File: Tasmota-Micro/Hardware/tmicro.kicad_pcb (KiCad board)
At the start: 2 copper layers, 33.5 x 13 mm, 16 parts, among them P2 CONN_01X02, P3 CONN_01X02, P4 CONN_01X04, P5 CONN_01X02, P6 CONN_01X02, P7 USB_A, Q1 IRLML6244, Q2 IRLML6244, U1 MCP1703, U2 ESP-01v090

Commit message: removed the confusing cache form the name
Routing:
- net Net-(R3-Pad1): track 11.1 -> 7.77 mm
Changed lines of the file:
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@@
 (kicad_pcb (version 4) (host pcbnew 4.0.2+dfsg1-stable)
   (general
-    (links 31)
-    (no_connects 1)
+    (links 0)
+    (no_connects 0)
     (area 144.407 102.575 201.425001 126.875)
     (thickness 1.6)
     (drawings 14)
-    (tracks 99)
+    (tracks 97)
     (zones 0)
     (modules 16)
@@
   (segment (start 169.95 115.201) (end 169.95 115.2008) (width 0.25) (layer F.Cu) (net 2) (status 30))
   (segment (start 158.22502 115.12502) (end 158.22502 115.010088) (width 0.4) (layer B.Cu) (net 3))
-  (segment (start 159.4 115.25) (end 158.35 115.25) (width 0.4) (layer B.Cu) (net 3))
+  (segment (start 159.4 115.25) (end 158.35 115.25) (width 0.4) (layer B.Cu) (net 3) (status 10))
   (via (at 158.22502 115.010088) (size 0.6) (drill 0.4) (layers F.Cu B.Cu) (net 3))
   (segment (start 158.35 115.25) (end 158.22502 115.12502) (width 0.4) (layer B.Cu) (net 3))
@@
   (segment (start 152.1 111.1664) (end 152.5464 110.72) (width 0.25) (layer F.Cu) (net 7))
   (segment (start 152.5464 110.72) (end 153.66 110.72) (width 0.25) (layer F.Cu) (net 7) (status 20))
-  (segment (start 165.58 118.8) (end 165.58 117.534) (width 0.25) (layer B.Cu) (net 8))
+  (segment (start 165.58 118.8) (end 165.58 117.534) (width 0.25) (layer B.Cu) (net 8) (status 10))
   (segment (start 165.58 117.534) (end 165.246 117.2) (width 0.25) (layer B.Cu) (net 8))
   (segment (start 165.246 117.2) (end 159 117.2) (width 0.25) (layer B.Cu) (net 8))
-  (segment (start 157.6 114.66) (end 156.2 113.26) (width 0.25) (layer B.Cu) (net 8))
+  (segment (start 157.6 114.66) (end 156.2 113.26) (width 0.25) (layer B.Cu) (net 8) (status 20))
   (segment (start 159 117.2) (end 157.6 115.8) (width 0.25) (layer B.Cu) (net 8))
   (segment (start 157.6 115.8) (end 157.6 114.66) (width 0.25) (layer B.Cu) (net 8))
@@
   (segment (start 177.8998 113.202) (end 174.848 113.202) (width 0.8) (layer F.Cu) (net 11) (status 30))
   (segment (start 177.8998 113.202) (end 177.9 113.2018) (width 0.25) (layer F.Cu) (net 11) (status 30))
-  (segment (start 154.5517 112.0711) (end 153.66 112.0711) (width 0.25) (layer B.Cu) (net 12))
-  (segment (start 154.8489 111.7739) (end 154.5517 112.0711) (width 0.25) (layer B.Cu) (net 12))
-  (segment (start 154.8489 110.3662) (end 154.8489 111.7739) (width 0.25) (layer B.Cu) (net 12))
-  (segment (start 155.6966 109.5185) (end 154.8489 110.3662) (width 0.25) (layer B.Cu) (net 12))
-  (segment (start 156.7485 109.5185) (end 155.6966 109.5185) (width 0.25) (layer B.Cu) (net 12))
-  (segment (start 159.4 112.17) (end 156.7485 109.5185) (width 0.25) (layer B.Cu) (net 12))
-  (segment (start 159.4 113.35) (end 159.4 112.17) (width 0.25) (layer B.Cu) (net 12) (status 10))
-  (segment (start 153.66 113.26) (end 153.66 112.0711) (width 0.25) (layer B.Cu) (net 12) (status 10))
+  (segment (start 158.7 111.6) (end 159.4 112.3) (width 0.25) (layer B.Cu) (net 12))
+  (segment (start 159.4 112.3) (end 159.4 113.35) (width 0.25) (layer B.Cu) (net 12))
+  (segment (start 157.8 111.6) (end 158.7 111.6) (width 0.25) (layer B.Cu) (net 12))
+  (segment (start 157.4 112) (end 157.8 111.6) (width 0.25) (layer B.Cu) (net 12))
+  (segment (start 154.92 112) (end 157.4 112) (width 0.25) (layer B.Cu) (net 12))
+  (segment (start 153.66 113.26) (end 154.92 112) (width 0.25) (layer B.Cu) (net 12))
   (segment (start 180.2 111.6) (end 180.8 111) (width 1.2) (layer B.Cu) (net 13) (status 20))
   (segment (start 178.099 111.6) (end 180.2 111.6) (width 1.2) (layer B.Cu) (net 13))

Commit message: updated with better zone fills
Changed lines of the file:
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@@
 (kicad_pcb (version 4) (host pcbnew 4.0.2+dfsg1-stable)
   (general
-    (links 0)
+    (links 31)
     (no_connects 0)
     (area 144.407 102.575 201.425001 126.875)
@@
     (user_trace_width 1.2)
     (trace_clearance 0.2)
-    (zone_clearance 0.2)
+    (zone_clearance 0.25)
     (zone_45_only no)
     (trace_min 0.2)
@@
   (gr_line (start 184.9 121) (end 184.9 108) (layer Edge.Cuts) (width 0.15))
   (segment (start 167.26 110.2) (end 169.8 110.2) (width 1.2) (layer B.Cu) (net 1) (status 30))
-  (segment (start 173.601 114.001) (end 169.8 110.2) (width 1.2) (layer B.Cu) (net 1) (status 30))
+  (segment (start 173.601 114.001) (end 169.8 110.2) (width 1.6) (layer B.Cu) (net 1) (status 30))
   (segment (start 173.601 114.2) (end 173.601 114.001) (width 1.2) (layer B.Cu) (net 1) (status 30))
   (segment (start 167.26 112.016) (end 167.26 110.2) (width 0.8) (layer F.Cu) (net 1) (status 20))
@@
   (segment (start 177.599 114.2) (end 177.599 112.1) (width 1.2) (layer B.Cu) (net 13) (status 10))
   (zone (net 2) (net_name GND) (layer B.Cu) (hatch edge 0.508)
-    (connect_pads yes (clearance 0.2))
+    (connect_pads yes (clearance 0.25))
     (min_thickness 0.2)
-    (fill yes (arc_segments 16) (thermal_gap 0.508) (thermal_bridge_width 0.508))
+    (fill yes (arc_segments 32) (thermal_gap 0.508) (thermal_bridge_width 0.508))
     (polygon
       (pts
@@
   )
   (zone (net 1) (net_name VPP) (layer F.Cu) (hatch edge 0.508)
-    (connect_pads yes (clearance 0.2))
+    (connect_pads yes (clearance 0.25))
     (min_thickness 0.2)
-    (fill yes (arc_segments 16) (thermal_gap 0.508) (thermal_bridge_width 0.508))
+    (fill yes (arc_segments 32) (thermal_gap 0.508) (thermal_bridge_width 0.508))
     (polygon
       (pts
@@
   )
   (zone (net 3) (net_name +3V3) (layer F.Cu) (hatch edge 0.508)
-    (connect_pads yes (clearance 0.2))
+    (connect_pads yes (clearance 0.25))
     (min_thickness 0.2)
-    (fill yes (arc_segments 16) (thermal_gap 0.508) (thermal_bridge_width 0.508))
+    (fill yes (arc_segments 32) (thermal_gap 0.508) (thermal_bridge_width 0.508))
     (polygon
       (pts

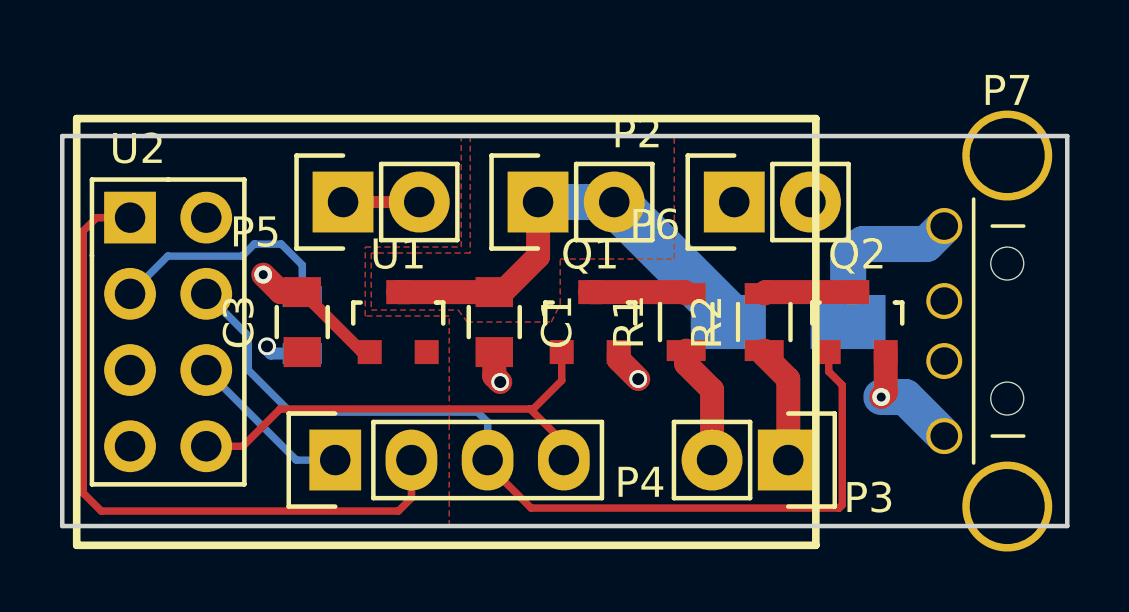
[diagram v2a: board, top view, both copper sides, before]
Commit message: 4 layers
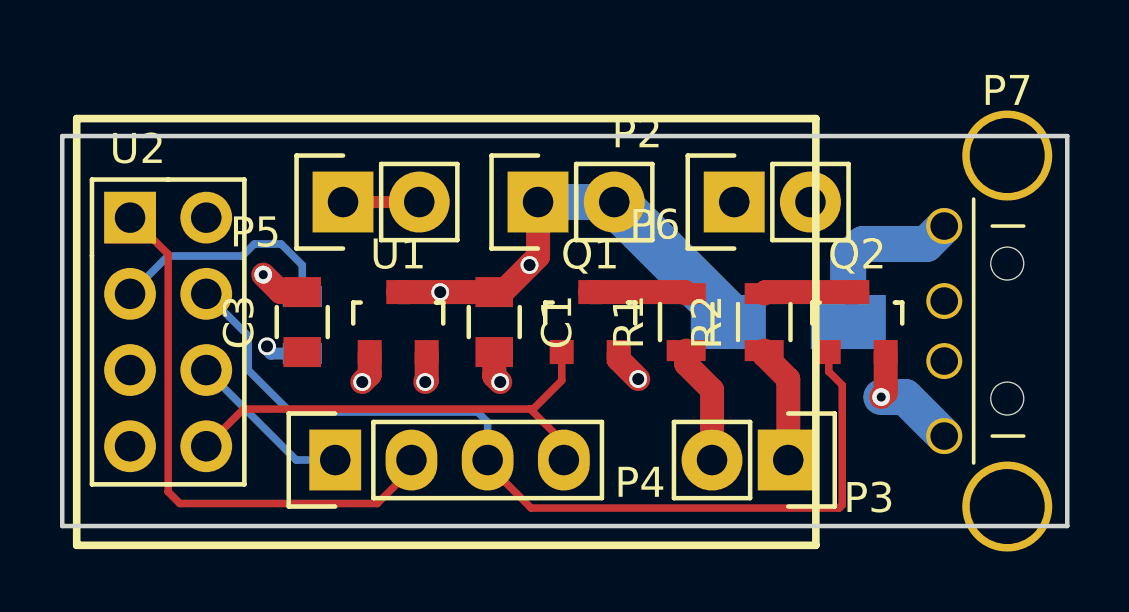
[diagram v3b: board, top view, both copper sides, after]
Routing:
- net TX: track 23.1 -> 19.8 mm
- net GND: track 11.4 -> 9.39 mm, vias 4 -> 5
- net +3V3: track 4.73 -> 5.75 mm, vias 1 -> 2
- net VPP: vias 0 -> 2
- added copper zone on In1.Cu, net +3V3
- added copper zone on In2.Cu, net GND
- added copper zone on In1.Cu, net VPP
- removed copper zone on F.Cu, net +3V3
- removed copper zone on B.Cu, net GND
- removed copper zone on F.Cu, net VPP
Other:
- copper layers 2 -> 4
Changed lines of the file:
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@@
   (general
     (links 31)
-    (no_connects 0)
+    (no_connects 1)
     (area 144.407 102.575 201.425001 126.875)
     (thickness 1.6)
     (drawings 14)
-    (tracks 97)
+    (tracks 107)
     (zones 0)
     (modules 16)
@@
   (layers
     (0 F.Cu signal)
+    (1 In1.Cu signal)
+    (2 In2.Cu signal)
     (31 B.Cu signal)
     (32 B.Adhes user)
@@
     (34 B.Paste user)
     (35 F.Paste user)
-    (36 B.SilkS user hide)
-    (37 F.SilkS user hide)
+    (36 B.SilkS user)
+    (37 F.SilkS user)
     (38 B.Mask user)
     (39 F.Mask user)
@@
   (gr_line (start 184.9 108) (end 151.4 108) (layer Edge.Cuts) (width 0.15))
   (gr_line (start 184.9 121) (end 184.9 108) (layer Edge.Cuts) (width 0.15))
+  (via (at 166.976 112.3) (size 0.6) (drill 0.4) (layers F.Cu B.Cu) (net 1))
+  (via (at 164 113.202) (size 0.6) (drill 0.4) (layers F.Cu B.Cu) (net 1))
+  (segment (start 166.976 112.3) (end 167.26 112.016) (width 0.8) (layer F.Cu) (net 1))
+  (segment (start 166.076 113.2) (end 166.976 112.3) (width 0.8) (layer F.Cu) (net 1) (status 10))
+  (segment (start 164 113.202) (end 165.798 113.202) (width 0.8) (layer F.Cu) (net 1) (status 20))
+  (segment (start 162.6002 113.202) (end 164 113.202) (width 0.8) (layer F.Cu) (net 1) (status 10))
   (segment (start 167.26 110.2) (end 169.8 110.2) (width 1.2) (layer B.Cu) (net 1) (status 30))
   (segment (start 173.601 114.001) (end 169.8 110.2) (width 1.6) (layer B.Cu) (net 1) (status 30))
   (segment (start 173.601 114.2) (end 173.601 114.001) (width 1.2) (layer B.Cu) (net 1) (status 30))
   (segment (start 167.26 112.016) (end 167.26 110.2) (width 0.8) (layer F.Cu) (net 1) (status 20))
-  (segment (start 166.076 113.2) (end 167.26 112.016) (width 0.8) (layer F.Cu) (net 1) (status 10))
   (segment (start 165.8 113.2) (end 166.076 113.2) (width 0.8) (layer F.Cu) (net 1) (status 30))
   (segment (start 162.6 113.202) (end 162.6002 113.202) (width 0.8) (layer F.Cu) (net 1) (status 30))
   (segment (start 165.798 113.202) (end 165.8 113.2) (width 0.8) (layer F.Cu) (net 1) (status 30))
-  (segment (start 162.6002 113.202) (end 165.798 113.202) (width 0.8) (layer F.Cu) (net 1) (status 30))
   (segment (start 162.6002 113.202) (end 162.6 113.2018) (width 0.25) (layer F.Cu) (net 1) (status 30))
-  (segment (start 161.65 115.20076) (end 161.40076 115.20076) (width 0.4) (layer F.Cu) (net 2) (status 30))
-  (segment (start 161.40076 115.20076) (end 159.4 113.2) (width 0.4) (layer F.Cu) (net 2) (status 30))
+  (segment (start 161.65 115.20076) (end 161.65 115.95) (width 0.8) (layer F.Cu) (net 2) (status 10))
+  (segment (start 161.65 115.95) (end 161.4 116.2) (width 0.8) (layer F.Cu) (net 2))
+  (via (at 161.4 116.2) (size 0.6) (drill 0.4) (layers F.Cu B.Cu) (net 2))
   (segment (start 161.65 115.20076) (end 161.60076 115.20076) (width 0.4) (layer F.Cu) (net 2) (status 30))
   (segment (start 169.95 115.20076) (end 169.95 115.45) (width 0.8) (layer F.Cu) (net 2) (status 30))
@@
   (segment (start 178.85 115.201) (end 178.85 115.2008) (width 0.25) (layer F.Cu) (net 2) (status 30))
   (segment (start 169.95 115.201) (end 169.95 115.2008) (width 0.25) (layer F.Cu) (net 2) (status 30))
+  (segment (start 163.55 115.20076) (end 163.55 116.15) (width 0.8) (layer F.Cu) (net 3) (status 10))
+  (segment (start 163.55 116.15) (end 163.5 116.2) (width 0.8) (layer F.Cu) (net 3))
+  (via (at 163.5 116.2) (size 0.6) (drill 0.4) (layers F.Cu B.Cu) (net 3))
   (segment (start 158.22502 115.12502) (end 158.22502 115.010088) (width 0.4) (layer B.Cu) (net 3))
   (segment (start 159.4 115.25) (end 158.35 115.25) (width 0.4) (layer B.Cu) (net 3) (status 10))
@@
   (segment (start 159.2 118.8) (end 156.2 115.8) (width 0.25) (layer B.Cu) (net 6) (status 20))
   (segment (start 160.5 118.8) (end 159.2 118.8) (width 0.25) (layer B.Cu) (net 6) (status 10))
-  (segment (start 163.04 120.066) (end 162.606 120.5) (width 0.25) (layer F.Cu) (net 7))
-  (segment (start 163.04 118.8) (end 163.04 120.066) (width 0.25) (layer F.Cu) (net 7) (status 10))
-  (segment (start 162.606 120.5) (end 152.7 120.5) (width 0.25) (layer F.Cu) (net 7))
-  (segment (start 152.7 120.5) (end 152.1 119.9) (width 0.25) (layer F.Cu) (net 7))
-  (segment (start 152.1 119.9) (end 152.1 111.1664) (width 0.25) (layer F.Cu) (net 7))
-  (segment (start 152.1 111.1664) (end 152.5464 110.72) (width 0.25) (layer F.Cu) (net 7))
-  (segment (start 152.5464 110.72) (end 153.66 110.72) (width 0.25) (layer F.Cu) (net 7) (status 20))
+  (segment (start 153.66 110.72) (end 153.71 110.72) (width 0.25) (layer F.Cu) (net 7))
+  (segment (start 155.32 120.25) (end 161.9 120.25) (width 0.25) (layer F.Cu) (net 7))
+  (segment (start 153.71 110.72) (end 154.93 111.94) (width 0.25) (layer F.Cu) (net 7))
+  (segment (start 154.93 111.94) (end 154.93 119.86) (width 0.25) (layer F.Cu) (net 7))
+  (segment (start 154.93 119.86) (end 155.32 120.25) (width 0.25) (layer F.Cu) (net 7))
+  (segment (start 163.04 119.11) (end 163.04 118.8) (width 0.25) (layer F.Cu) (net 7))
+  (segment (start 161.9 120.25) (end 163.04 119.11) (width 0.25) (layer F.Cu) (net 7))
+  (segment (start 153.66 110.72) (end 153.66 110.86) (width 0.25) (layer F.Cu) (net 7) (status 30))
+  (segment (start 163.04 117.94) (end 163.04 118.8) (width 0.25) (layer F.Cu) (net 7) (status 30))
+  (segment (start 163.04 118.8) (end 162.964602 118.8) (width 0.25) (layer F.Cu) (net 7) (status 30))
   (segment (start 165.58 118.8) (end 165.58 117.534) (width 0.25) (layer B.Cu) (net 8) (status 10))
   (segment (start 165.58 117.534) (end 165.246 117.2) (width 0.25) (layer B.Cu) (net 8))
@@
   (segment (start 177.3 120.4) (end 167.0276 120.4) (width 0.25) (layer F.Cu) (net 8))
   (segment (start 167.0276 120.4) (end 165.58 118.9524) (width 0.25) (layer F.Cu) (net 8) (status 20))
+  (segment (start 167 117.1) (end 157.44 117.1) (width 0.25) (layer F.Cu) (net 9))
+  (segment (start 157.44 117.1) (end 156.2 118.34) (width 0.25) (layer F.Cu) (net 9))
   (segment (start 167 117.1) (end 167.1 117.1) (width 0.25) (layer F.Cu) (net 9))
   (segment (start 167.1 117.1) (end 168.05 116.15) (width 0.25) (layer F.Cu) (net 9))
   (segment (start 168.05 116.15) (end 168.05 115.20076) (width 0.25) (layer F.Cu) (net 9) (status 20))
-  (segment (start 158.661314 117.1) (end 167 117.1) (width 0.25) (layer F.Cu) (net 9))
   (segment (start 167 117.1) (end 168.12 118.22) (width 0.25) (layer F.Cu) (net 9) (status 20))
   (segment (start 168.12 118.22) (end 168.12 118.8) (width 0.25) (layer F.Cu) (net 9) (status 30))
   (segment (start 168.12 118.6476) (end 168.12 118.8) (width 0.25) (layer F.Cu) (net 9) (status 30))
-  (segment (start 156.2 118.34) (end 157.421314 118.34) (width 0.25) (layer F.Cu) (net 9) (status 10))
-  (segment (start 157.421314 118.34) (end 158.661314 117.1) (width 0.25) (layer F.Cu) (net 9))
   (segment (start 168.05 118.73) (end 168.12 118.8) (width 0.25) (layer F.Cu) (net 9) (status 30))
   (segment (start 169 113.202) (end 169.0002 113.202) (width 0.8) (layer F.Cu) (net 10) (status 30))
@@
   (segment (start 177.8998 113.202) (end 177.9 113.2018) (width 0.25) (layer F.Cu) (net 11) (status 30))
   (segment (start 158.7 111.6) (end 159.4 112.3) (width 0.25) (layer B.Cu) (net 12))
-  (segment (start 159.4 112.3) (end 159.4 113.35) (width 0.25) (layer B.Cu) (net 12))
+  (segment (start 159.4 112.3) (end 159.4 113.35) (width 0.25) (layer B.Cu) (net 12) (status 20))
   (segment (start 157.8 111.6) (end 158.7 111.6) (width 0.25) (layer B.Cu) (net 12))
   (segment (start 157.4 112) (end 157.8 111.6) (width 0.25) (layer B.Cu) (net 12))
   (segment (start 154.92 112) (end 157.4 112) (width 0.25) (layer B.Cu) (net 12))
-  (segment (start 153.66 113.26) (end 154.92 112) (width 0.25) (layer B.Cu) (net 12))
+  (segment (start 153.66 113.26) (end 154.92 112) (width 0.25) (layer B.Cu) (net 12) (status 10))
   (segment (start 180.2 111.6) (end 180.8 111) (width 1.2) (layer B.Cu) (net 13) (status 20))
   (segment (start 178.099 111.6) (end 180.2 111.6) (width 1.2) (layer B.Cu) (net 13))
   (segment (start 177.599 112.1) (end 178.099 111.6) (width 1.2) (layer B.Cu) (net 13))
   (segment (start 177.599 114.2) (end 177.599 112.1) (width 1.2) (layer B.Cu) (net 13) (status 10))
-  (zone (net 2) (net_name GND) (layer B.Cu) (hatch edge 0.508)
+  (zone (net 2) (net_name GND) (layer In2.Cu) (hatch edge 0.508)
     (connect_pads yes (clearance 0.25))
     (min_thickness 0.2)
@@
     )
   )
-  (zone (net 1) (net_name VPP) (layer F.Cu) (hatch edge 0.508)
+  (zone (net 1) (net_name VPP) (layer In1.Cu) (hatch edge 0.508)
     (connect_pads yes (clearance 0.25))
     (min_thickness 0.2)
@@
     (polygon
       (pts
-        (xy 165 108) (xy 165 111.9) (xy 161.7 111.9) (xy 161.7 113.8) (xy 164.6 113.8)
+        (xy 165 108) (xy 165 112) (xy 161.7 112) (xy 161.7 113.8) (xy 164.6 113.8)
         (xy 164.9 114.2) (xy 167.7 114.2) (xy 168 113.6) (xy 168 112.1) (xy 171.8 112.1)
         (xy 171.8 108)
@@
     )
   )
-  (zone (net 3) (net_name +3V3) (layer F.Cu) (hatch edge 0.508)
+  (zone (net 3) (net_name +3V3) (layer In1.Cu) (hatch edge 0.508)
     (connect_pads yes (clearance 0.25))
     (min_thickness 0.2)
@@
     (polygon
       (pts
-        (xy 151.4 108) (xy 151.4 121) (xy 164.3 121) (xy 164.3 114) (xy 161.5 114)
-        (xy 161.5 111.7) (xy 164.7 111.7) (xy 164.7 108)
+        (xy 151.4 108) (xy 151.4 121) (xy 164.3 121) (xy 164.3 114.1) (xy 161.4 114.1)
+        (xy 161.4 111.7) (xy 164.7 111.7) (xy 164.7 108)
       )
     )
